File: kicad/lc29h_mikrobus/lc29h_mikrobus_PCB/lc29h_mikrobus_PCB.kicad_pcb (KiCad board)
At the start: 2 copper layers, 27.4 x 57.5 mm, 47 parts, among them IC1 MIKROE-924, IC101 DS28E36BQ+U, IC102 74LVC1G3157GV,125, J1 Conn_Coaxial, J2 Conn_01x03_Pin, Q1 DMP3013SFV, Q101 BC856B-13-F, Q102 BSS123L, Q3 BSS123L, Q4 PN2222A, SW101 SW_Nidec_CAS-120A1, U101 LC29H, U103 TXS0102DCU

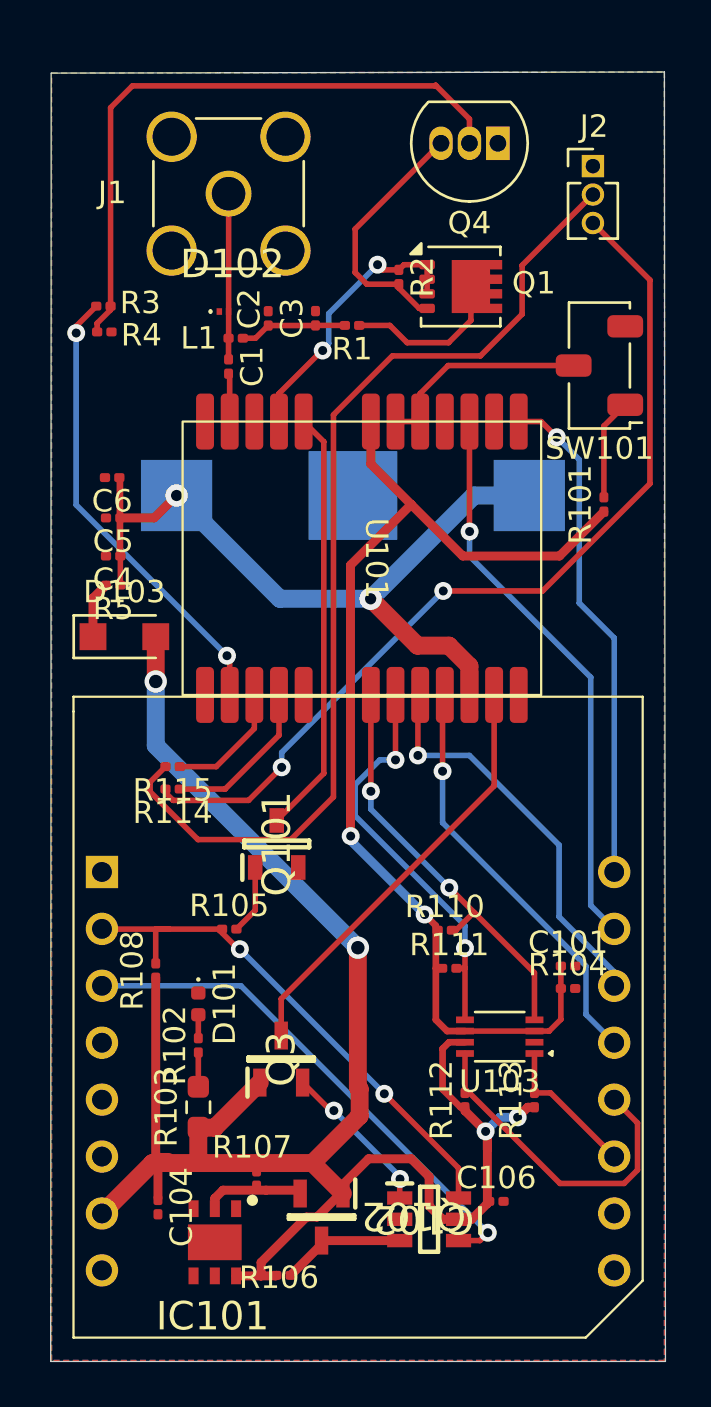
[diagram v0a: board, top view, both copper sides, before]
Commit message: remove all errors in Design Rule Check
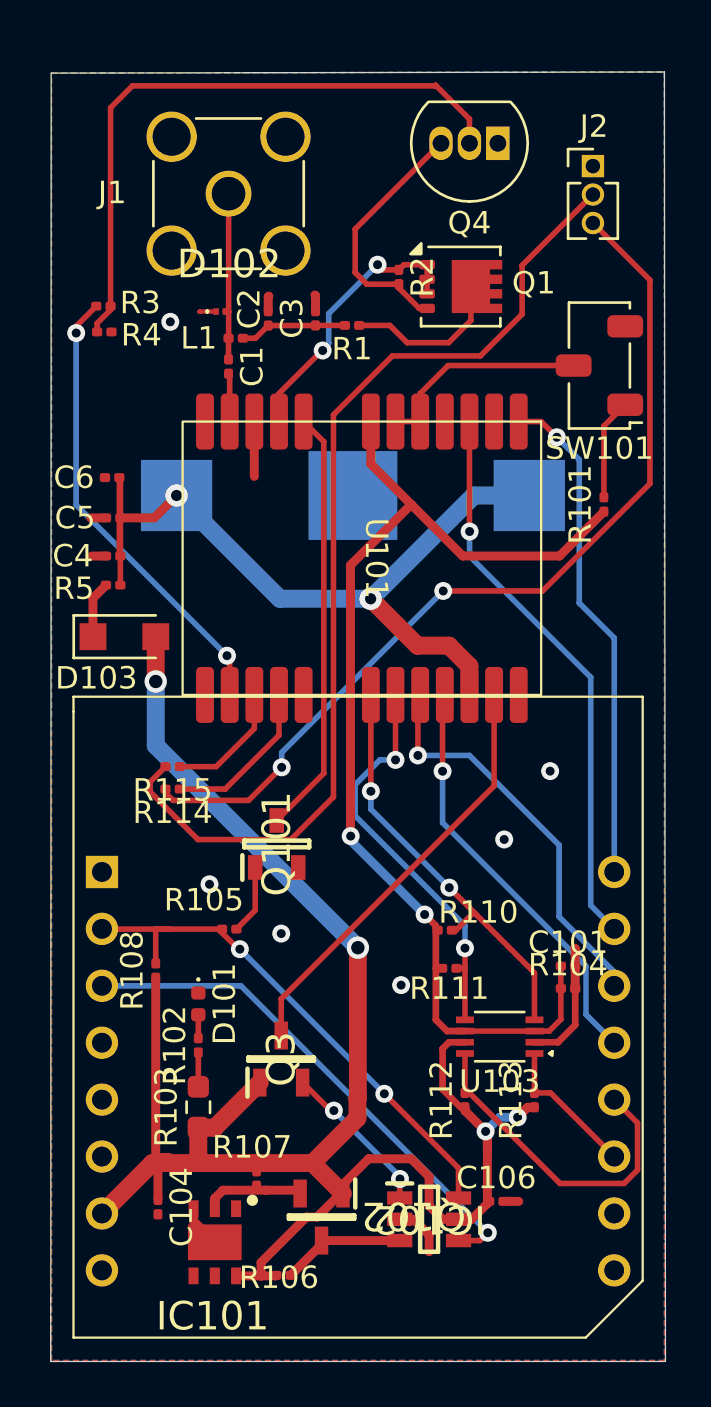
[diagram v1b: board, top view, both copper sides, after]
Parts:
- moved D102 0.14 mm to (131.4, 50.2)
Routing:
- net GND: track 0.00 -> 16.4 mm, vias 0 -> 6

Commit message: rearrange components and remove most warnings
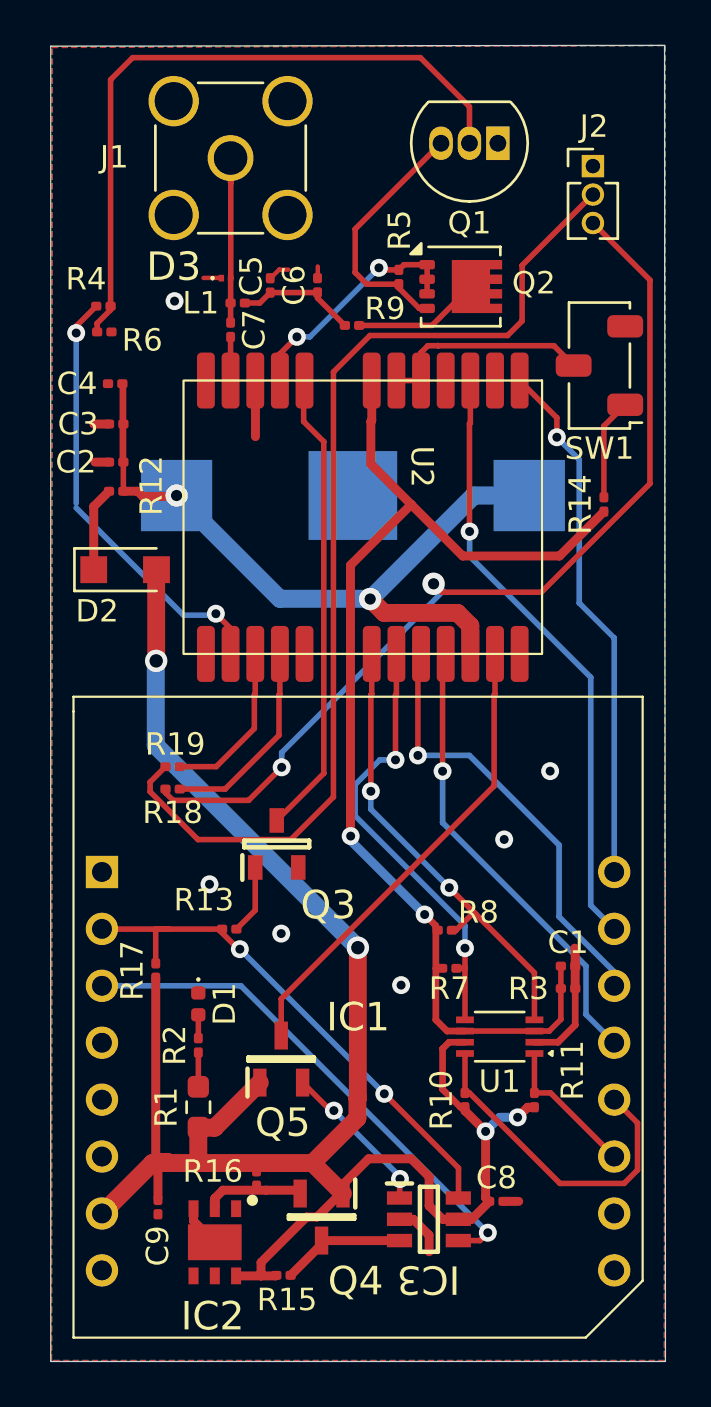
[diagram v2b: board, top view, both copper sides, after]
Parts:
- IC1: value MIKROE-924 -> MIKROE924
- moved C2 4.19 mm to (126.7, 56.9)
- moved C4 4.19 mm to (126.7, 53.4)
- moved C3 4.19 mm to (126.7, 55.2)
- moved R12 4.19 mm to (126.7, 58.2)
- moved D2 2.99 mm to (127.1, 61.7)
- moved U2 1.83 mm to (137.7, 59.4)
- moved C7 1.64 mm to (131.8, 51.0)
- moved J1 1.59 mm to (131.8, 43.4)
- moved L1 1.57 mm to (132.2, 49.8)
- moved D3 1.51 mm to (131.6, 48.7)
- moved C6 1.47 mm to (135.7, 49.0)
- moved C5 1.47 mm to (133.6, 49.0)
- renumbered C101 to C1, C4 to C2, C5 to C3, C6 to C4, C2 to C5, C3 to C6, C1 to C7, C106 to C8, C104 to C9, D101 to D1, D103 to D2, D102 to D3, IC101 to IC2, IC102 to IC3, Q4 to Q1, Q1 to Q2, Q101 to Q3, Q102 to Q4, Q3 to Q5, R103 to R1, R112 to R10, R113 to R11, R5 to R12, R105 to R13, R101 to R14, R106 to R15, R107 to R16, R108 to R17, R114 to R18, R115 to R19, R102 to R2, R104 to R3, R3 to R4, R2 to R5, R4 to R6, R111 to R7, R110 to R8, R1 to R9, SW101 to SW1, U103 to U1, U101 to U2
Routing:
- net VCC: track 85.2 -> 87.5 mm
- net Net-(Q1-B): track 28.4 -> 30.5 mm
- net 1PPS: track 25.2 -> 27.2 mm
- net VDD_EXT: track 49.2 -> 51.0 mm
- net mSDA: track 19.0 -> 20.8 mm
- net Net-(Q5-D): track 19.1 -> 21.0 mm
- net mSCL: track 18.1 -> 19.9 mm
- net Net-(U2-TXD2): track 5.53 -> 7.38 mm
- net Net-(U2-RXD2): track 7.22 -> 9.07 mm
- net Net-(Q3-C): track 19.0 -> 20.9 mm
- net VDD_RF: track 12.5 -> 10.8 mm
- net TX1: track 18.0 -> 19.6 mm
- net Net-(Q2-D): track 7.23 -> 5.70 mm
- net RX1: track 18.7 -> 20.2 mm
- net Net-(J2-Pin_2): track 45.2 -> 46.5 mm
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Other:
- board size 27.4 x 57.5 mm -> 27.4 x 58.7 mm

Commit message: BSS123L connections corrected and schematic commented
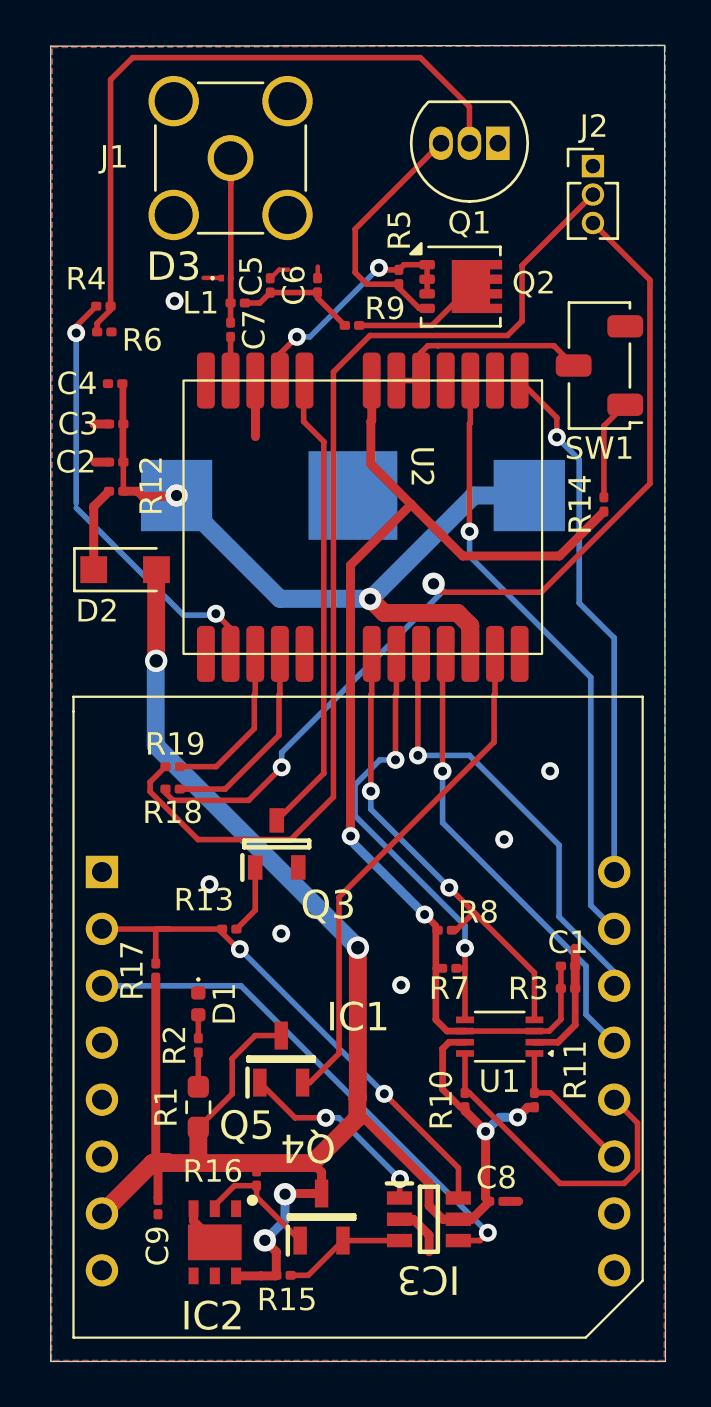
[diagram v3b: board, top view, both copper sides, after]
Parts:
- IC1: value MIKROE924 -> MIKROE-924
- turned Q4 to 90 degrees
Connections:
- Q4 pad 1: VCC -> Net-(IC2-IO)
- Q4 pad 2: Net-(IC2-IO) -> Net-(IC3-Y0)
- Q4 pad 3: Net-(IC3-Y0) -> VCC
- Q5 pad 1: VCC -> CE
- Q5 pad 2: CE -> Net-(Q5-S)
- Q5 pad 3: Net-(Q5-D) -> VCC
- U2 pad 23: Net-(Q5-D) -> Net-(Q5-S)
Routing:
- net Net-(Q5-S): track 0.00 -> 22.9 mm
- net Net-(Q5-D): track 21.0 -> 0.00 mm
- net VCC: track 87.5 -> 89.7 mm, vias 4 -> 6
- net CE: track 7.04 -> 8.99 mm
- net Net-(IC2-IO): track 4.45 -> 5.63 mm

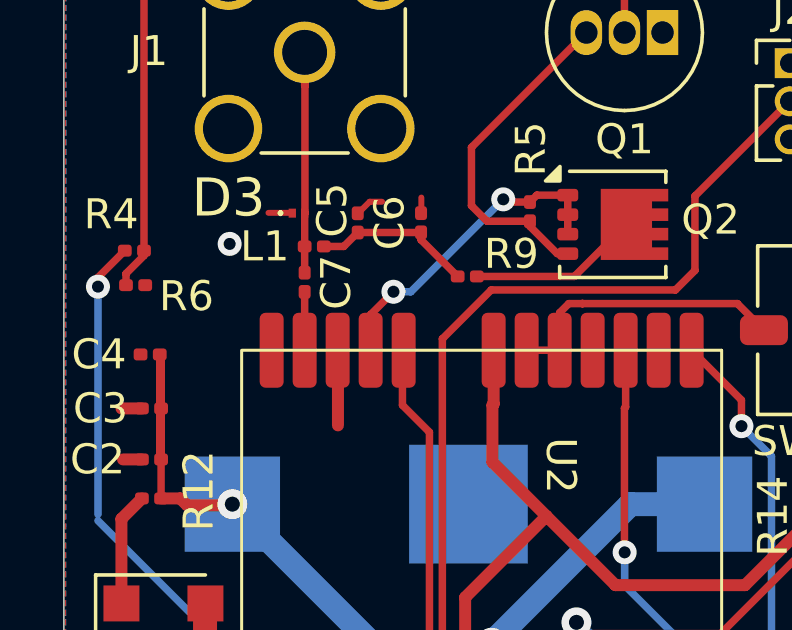
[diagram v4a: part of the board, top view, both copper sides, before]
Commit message: mass layer isolation adjusted
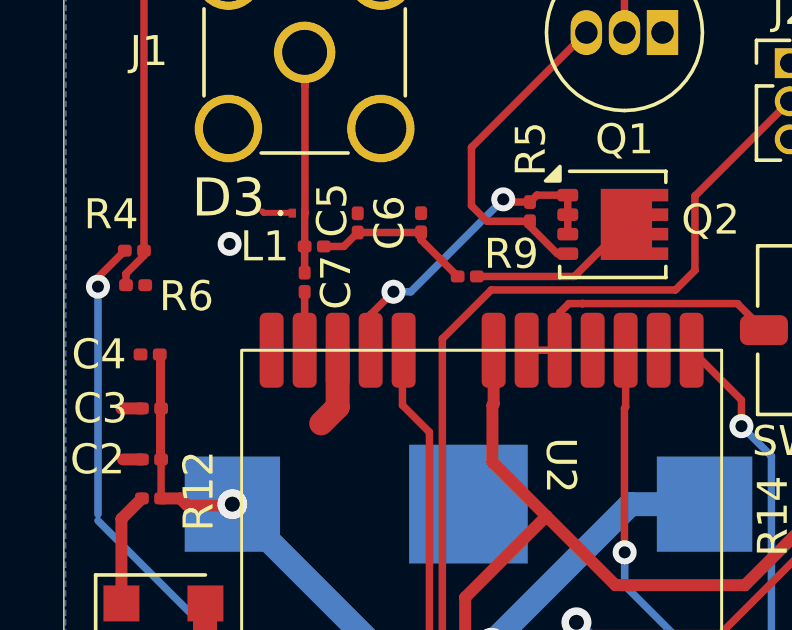
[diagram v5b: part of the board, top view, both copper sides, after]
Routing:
- net GND: track 16.5 -> 15.4 mm
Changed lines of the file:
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@@
-	)
-	(segment
-		(start 132.943 53.346)
-		(end 132.943 55.796)
-		(width 0.4)
-		(layer "F.Cu")
-		(net 1)
 	)
 	(segment
@@
 		(end 140.693 92.171)
 		(width 0.4)
-		(layer "F.Cu")
-		(net 1)
-	)
-	(segment
-		(start 134.413 48.341)
-		(end 134 48.341)
-		(width 0.2)
-		(layer "F.Cu")
-		(net 1)
-	)
-	(segment
-		(start 134 48.341)
-		(end 133.613 48.728)
-		(width 0.2)
 		(layer "F.Cu")
 		(net 1)
@@
 	)
 	(segment
-		(start 131.36 48.711)
-		(end 130.626 48.711)
-		(width 0.2)
-		(layer "F.Cu")
-		(net 1)
-	)
-	(segment
 		(start 144.013 89.921)
 		(end 144.693 89.921)
@@
 	)
 	(segment
-		(start 135.723 48.201)
-		(end 135.723 48.718)
-		(width 0.2)
+		(start 132.933 53.291)
+		(end 132.933 55.181)
+		(width 0.8)
+		(layer "F.Cu")
+		(net 1)
+	)
+	(segment
+		(start 132.933 55.181)
+		(end 132.383 55.731)
+		(width 0.8)
 		(layer "F.Cu")
 		(net 1)
@@
 		(end 147.193 78.621)
 		(width 0.4)
+		(layer "F.Cu")
+		(net 1)
+	)
+	(segment
+		(start 130.423 48.661)
+		(end 130.473 48.711)
+		(width 0.2)
 		(layer "F.Cu")
 		(net 1)
@@
 	)
 	(segment
+		(start 130.473 48.711)
+		(end 131.36 48.711)
+		(width 0.2)
+		(layer "F.Cu")
+		(net 1)
+	)
+	(segment
 		(start 139.983 90.721)
 		(end 140.683 91.421)
@@
 		(hatch edge 0.5)
 		(connect_pads
-			(clearance 0.508)
+			(clearance 0.25)
 		)
 		(min_thickness 0.25)

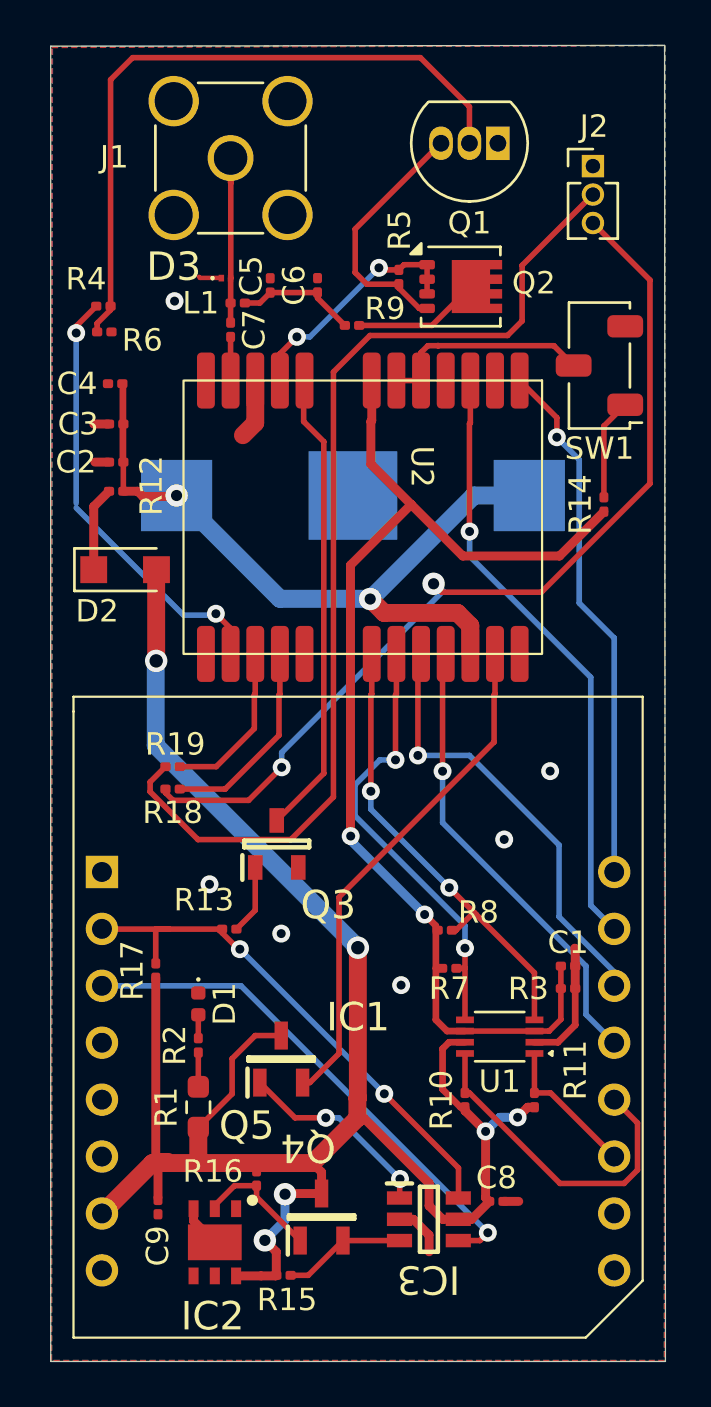
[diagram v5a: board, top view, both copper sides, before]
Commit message: replace all 201 SMD components with 805 for hand soldering
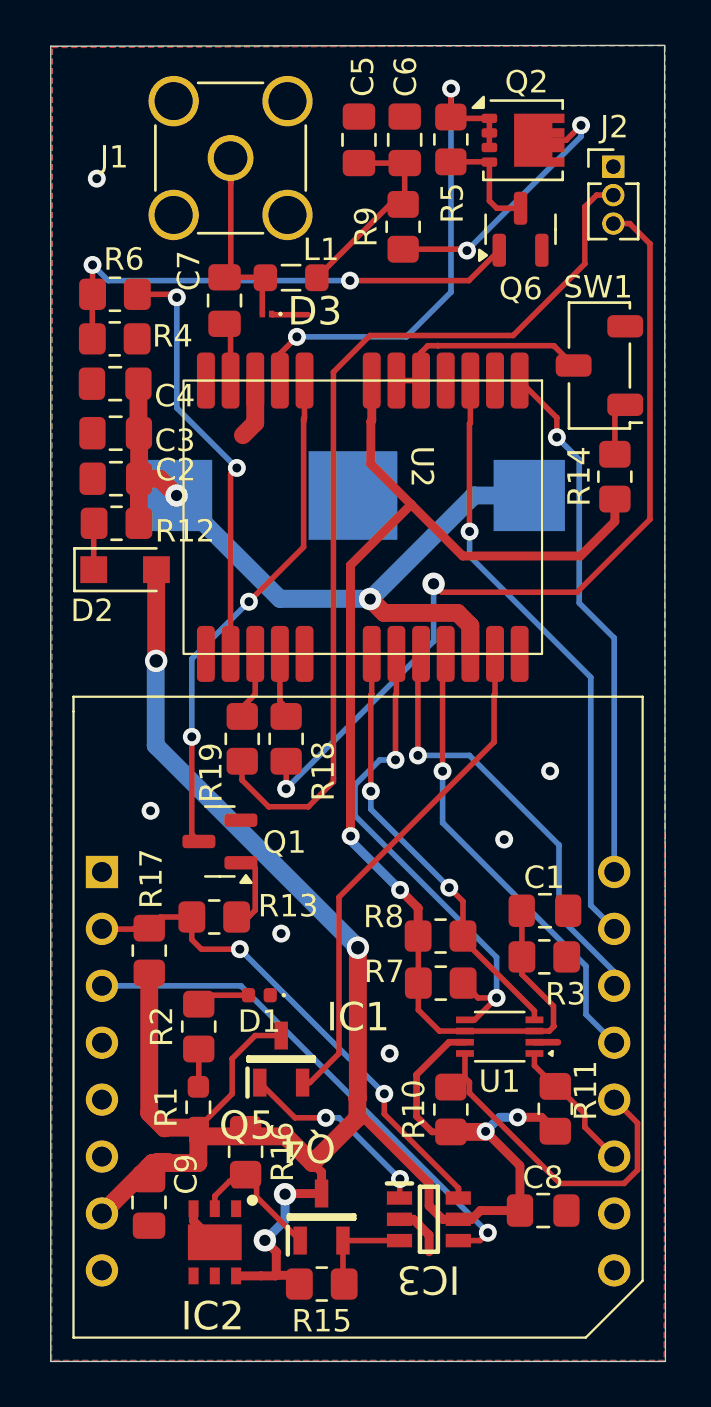
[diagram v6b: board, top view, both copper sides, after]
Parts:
- removed G***: LOGO, Logos-image:Image-Csug_6x6
- removed Q3: BC856B-13-F, BC856B-13-F:SOT96P240X110-3N
- added Q6: MMBT2222A, Package_TO_SOT_SMD:SOT-23, F.Cu at (144.8, 46.5)
- C1, C2, C3, C4, C5, C6, C7, C8, C9: footprint Capacitor_SMD:C_0201_0603Metric -> Capacitor_SMD:C_0805_2012Metric_Pad1.18x1.45mm_HandSolder
- L1: footprint Inductor_SMD:L_0201_0603Metric -> Inductor_SMD:L_0805_2012Metric_Pad1.05x1.20mm_HandSolder
- Q1: value PN2222A -> MMBT2222A; footprint Package_TO_SOT_THT:TO-92_Inline -> Package_TO_SOT_SMD:SOT-23
- R10, R11, R7, R8: value 4.7k -> 10k; footprint Resistor_SMD:R_0201_0603Metric -> Resistor_SMD:R_0805_2012Metric_Pad1.20x1.40mm_HandSolder
- R12, R13, R14, R15, R16, R17, R18, R19, R2, R3, R4, R5, R6, R9: footprint Resistor_SMD:R_0201_0603Metric -> Resistor_SMD:R_0805_2012Metric_Pad1.20x1.40mm_HandSolder
- moved Q1 33.5 mm to (131.4, 73.9)
- moved C5 7.61 mm to (137.6, 42.5)
- moved C6 7.57 mm to (139.6, 42.5)
- moved Q2 7.10 mm to (144.9, 42.6)
- moved R5 6.56 mm to (141.7, 42.5)
- moved R18 5.54 mm to (134.3, 69.3), turned to -90 degrees
- moved R9 4.96 mm to (139.5, 46.4), turned to 90 degrees
- moved R19 3.34 mm to (132.4, 69.3), turned to -90 degrees
- moved D1 2.75 mm to (133.1, 80.7), turned to 180 degrees
- moved C1 2.68 mm to (145.9, 77.0)
- moved L1 2.63 mm to (134.5, 48.7)
- moved D3 2.43 mm to (133.5, 50.3), turned to 180 degrees
- moved C8 2.13 mm to (145.8, 90.3)
- moved R3 1.76 mm to (145.8, 79.0)
- moved R15 1.75 mm to (135.9, 93.6)
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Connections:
- Q1 pad 1: GND -> Net-(Q1-B)
- Q1 pad 2: Net-(Q1-B) -> GND
- Q2 pad 4: Net-(Q1-C) -> Net-(Q2-G)
- R13 pad 2: Net-(Q3-B) -> Net-(Q1-B)
- R4 pad 2: Net-(Q1-B) -> Net-(Q6-B)
- R5 pad 2: Net-(Q1-C) -> Net-(Q2-G)
- R6 pad 1: Net-(Q1-B) -> Net-(Q6-B)
- U2 pad 8: Net-(Q3-C) -> Net-(Q1-C)
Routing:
- net Net-(Q1-B): track 30.5 -> 2.86 mm
- net Net-(Q6-B): track 0.00 -> 22.3 mm, vias 0 -> 2
- net Net-(Q3-C): track 20.9 -> 0.00 mm
- net VDD_RF: track 10.8 -> 23.4 mm
- net Net-(Q1-C): track 11.3 -> 23.0 mm, vias 0 -> 2
- net VCC: track 89.7 -> 97.8 mm
- net Net-(Q2-D): track 5.70 -> 13.0 mm, vias 0 -> 2
- net Net-(U2-RXD2): track 9.07 -> 2.51 mm
- net GND: track 15.4 -> 9.60 mm
- net Net-(Q2-G): track 0.00 -> 4.98 mm
- net Net-(U2-TXD2): track 7.38 -> 2.63 mm
- net Net-(J2-Pin_2): track 46.5 -> 41.8 mm
- net VDD_EXT: track 51.0 -> 55.2 mm
- net Net-(C5-Pad1): track 5.41 -> 9.12 mm
- net Net-(Q3-B): track 3.10 -> 0.00 mm
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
